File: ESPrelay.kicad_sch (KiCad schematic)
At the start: 26 parts, among them J1 Screw_Terminal, J3 USB_C_Receptacle_USB2.0_14P, K1 Relay_SPDT_Latching_1coil, K2 Relay_SPDT_Latching_1coil, K3 Relay_SPDT_Latching_1coil, K4 Relay_SPDT_Latching_1coil, K5 Relay_SPDT_Latching_1coil, K6 Relay_SPDT_Latching_1coil, K7 Relay_SPDT_Latching_1coil, K8 Relay_SPDT_Latching_1coil, U1 ESP32-S3-WROOM-1, U2 ULN2803A, U4 L7805, U5 LF33_TO252

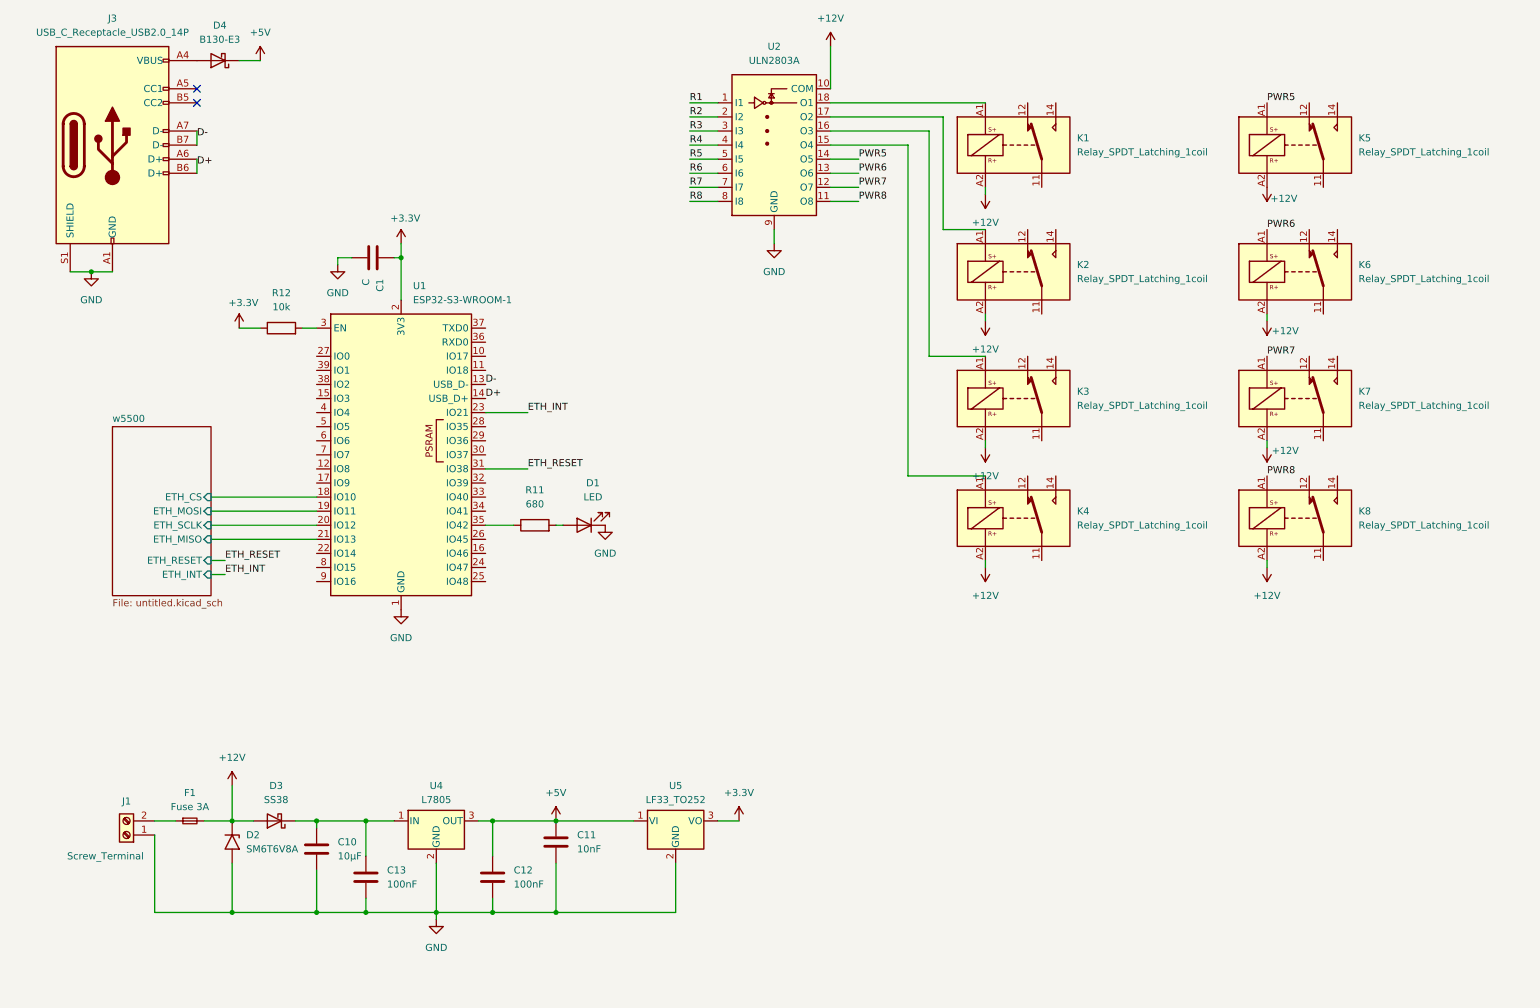
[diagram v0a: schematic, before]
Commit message: avancement carte 4 relays
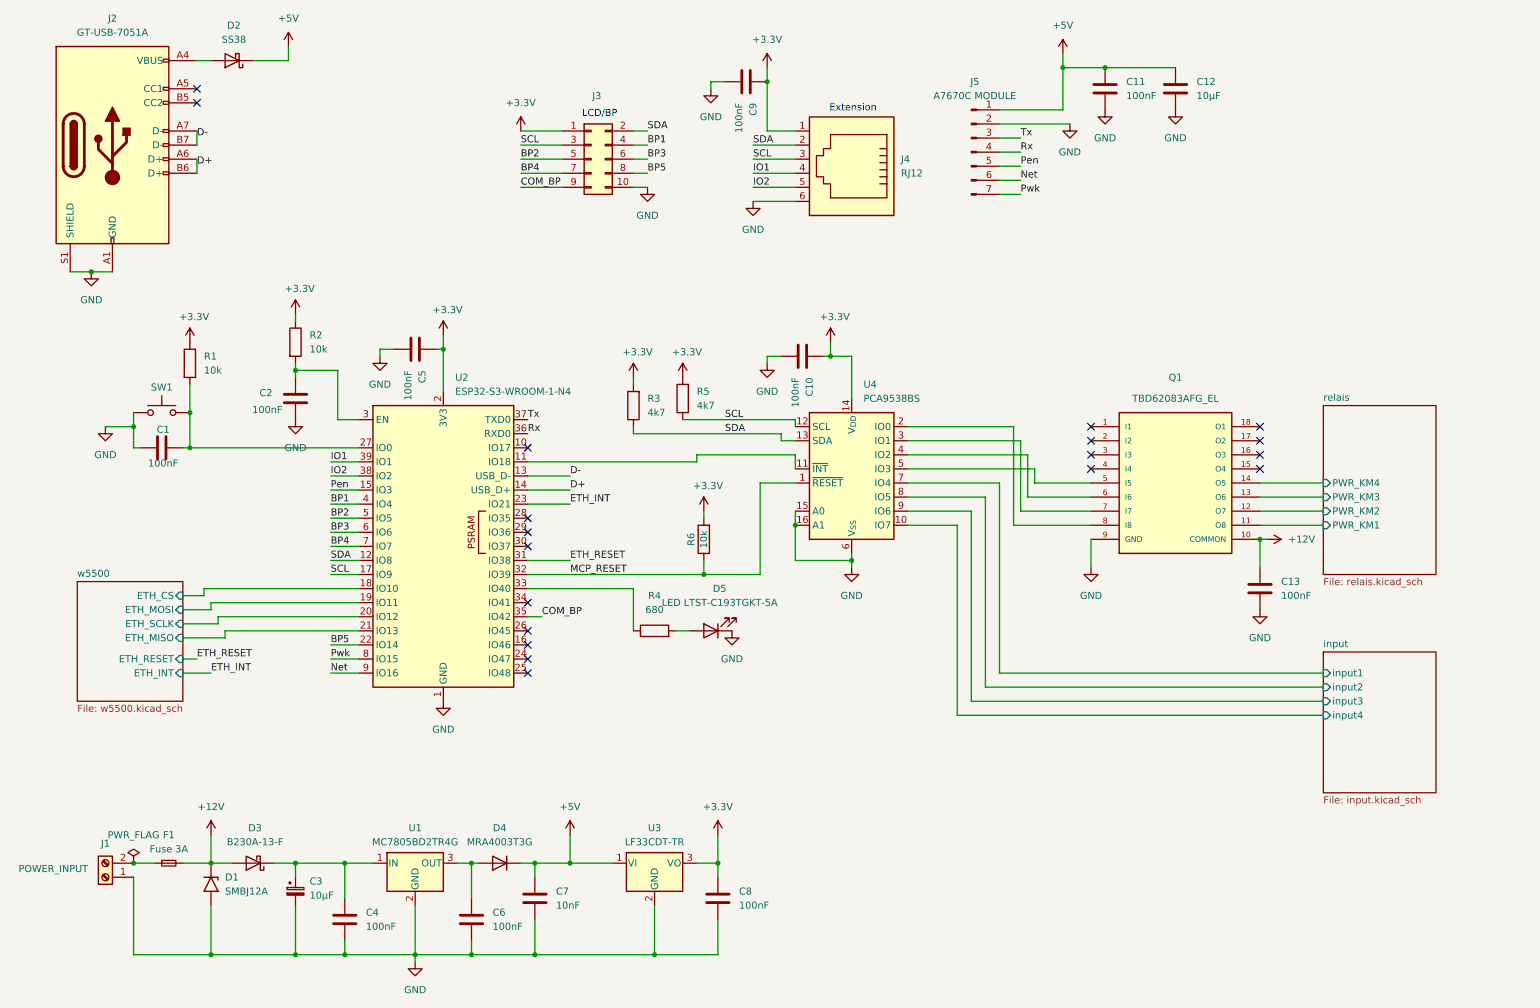
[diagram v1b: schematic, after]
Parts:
- removed D4: B130-E3, Diode_SMD:D_SMA, symbol Diode:B130-E3
- removed K1, K2, K3, K4, K5, K6, K7, K8: Relay_SPDT_Latching_1coil, Relay_THT:Relay_SPDT_Schrack-RP-II-1-FormC_RM3.5mm, symbol Relay:Relay_SPDT_Latching_1coil
- removed U2: ULN2803A, Package_SO:SOIC-18W_7.5x11.6mm_P1.27mm, symbol Transistor_Array:ULN2803A
- added C1, C11, C13, C2, C8, C9: 100nF, Capacitor_SMD:C_0402_1005Metric, symbol Device:C
- added C12: 10µF, Capacitor_SMD:C_0805_2012Metric, symbol Device:C
- added C3: 10µF, Capacitor_SMD:CP_Elec_4x5.4, symbol Device:C_Polarized_Small
- added D2: SS38, Diode_SMD:D_SMA, symbol Diode:SS38
- added D4: MRA4003T3G, Diode_SMD:D_SMA, symbol Diode:MRA4003T3G
- added J3: LCD/BP, Connector_FFC-FPC:Molex_54548-1071_1x10-1MP_P0.5mm_Horizontal, symbol Connector_Generic:Conn_02x05_Odd_Even
- added J4: RJ12, Connector_RJ:RJ12_Amphenol_54601-x06_Horizontal, symbol Connector:RJ12
- added J5: A7670C MODULE, labotronik:a7670c module, symbol Connector:Conn_01x07_Pin
- added Q1: TBD62083AFG_EL, TBD62083AFG_EL:SOIC127P1030X245-18N, symbol TBD62083AFG_EL:TBD62083AFG_EL
- added R1, R6: 10k, Resistor_SMD:R_0402_1005Metric, symbol Device:R
- added R3, R5: 4k7, Resistor_SMD:R_0402_1005Metric, symbol Device:R
- added SW1: SW_Push, Button_Switch_SMD:SW_Tactile_SPST_NO_Straight_CK_PTS636Sx25SMTRLFS, symbol Switch:SW_Push
- added U4: PCA9538BS, Package_DFN_QFN:NXP_VQFN-16-1EP_4x4mm_P0.65mm_EP2.1x2.1mm, symbol Interface_Expansion:PCA9538BS
- C10: value 10µF -> 100nF; footprint (none) -> Capacitor_SMD:C_0402_1005Metric
- C4: renamed from C13; footprint (none) -> Capacitor_SMD:C_0402_1005Metric
- C5: renamed from C1; value C -> 100nF; footprint Capacitor_SMD:C_0805_2012Metric -> Capacitor_SMD:C_0402_1005Metric
- C6: renamed from C12; footprint (none) -> Capacitor_SMD:C_0402_1005Metric
- C7: renamed from C11; footprint (none) -> Resistor_SMD:R_0402_1005Metric
- D1: renamed from D2; value SM6T6V8A -> SMBJ12A
- D3: value SS38 -> B230A-13-F
- D5: renamed from D1; value LED -> LED LTST-C193TGKT-5A; footprint (none) -> LED_SMD:LED_0603_1608Metric
- F1: footprint Fuse:Fuse_1210_3225Metric -> labotronik:0154250DR littelfuse 10.62 3.81
- J1: value Screw_Terminal -> POWER_INPUT; footprint TerminalBlock:TerminalBlock_MaiXu_MX126-5.0-02P_1x02_P5.00mm -> Connector_Phoenix_MC:PhoenixContact_MCV_1,5_2-G-3.5_1x02_P3.50mm_Vertical
- J2: renamed from J3; value USB_C_Receptacle_USB2.0_14P -> GT-USB-7051A; footprint Connector_USB:USB_C_Receptacle_G-Switch_GT-USB-7010ASV -> Connector_USB:USB_C_Receptacle_G-Switch_GT-USB-7051x
- R2: renamed from R12; footprint (none) -> Resistor_SMD:R_0402_1005Metric
- R4: renamed from R11; footprint (none) -> Resistor_SMD:R_0402_1005Metric
- U1: renamed from U4; value L7805 -> MC7805BD2TR4G
- U2: renamed from U1; value ESP32-S3-WROOM-1 -> ESP32-S3-WROOM-1-N4
- U3: renamed from U5; value LF33_TO252 -> LF33CDT-TR
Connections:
- net +12V: now also C13.1, Q1.10 (COMMON)
- net +3.3V: now also C10.1, C8.1, C9.1, J3.1 (Pin_1), J4.1, R1.1, R3.2, R5.2, R6.2, U4.14 (V_{DD})
- net +5V: now also C11.1, C12.1, D2.1 (K), D4.1 (K), J5.1 (Pin_1); no longer C6.1, U1.3 (OUT)
- net GND: now also C1.2, C11.2, C12.2, C13.2, C2.2, C3.2, C8.2, C9.2, J3.10 (Pin_10), J4.6, J5.2 (Pin_2), Q1.9 (GND), SW1.1, U4.15 (A0), U4.16 (A1), U4.17 (V_{SS}), U4.6 (V_{SS})
- net at U2.11 (IO18): now also U4.11 (~{INT})
- net SDA: now reaches U2.12 (IO8)
- net SDA: now also J3.2 (Pin_2), J4.2, R3.1, U4.13 (SDA)
- net Pen: now reaches U2.15 (IO3)
- net Pen: now also J5.5 (Pin_5)
- net SCL: now reaches U2.17 (IO9)
- net SCL: now also J3.3 (Pin_3), J4.3, R5.1, U4.12 (SCL)
- net BP5: now reaches U2.22 (IO14)
- net BP5: now also J3.8 (Pin_8)
- net at U2.27 (IO0): now also C1.1, R1.2, SW1.2
- net at R2.2, U2.3 (EN): now also C2.1
- net MCP_RESET: now reaches U2.32 (IO39)
- net MCP_RESET: now also R6.1, U4.1 (~{RESET})
- net at U2.33 (IO40): now also R4.1
- net COM_BP: now reaches U2.35 (IO42)
- net COM_BP: now also J3.9 (Pin_9); no longer R4.1
- net Rx: now reaches U2.36 (RXD0)
- net Rx: now also J5.4 (Pin_4)
- net Tx: now reaches U2.37 (TXD0)
- net Tx: now also J5.3 (Pin_3)
- net IO2: now reaches U2.38 (IO2)
- net IO2: now also J4.5
- net IO1: now reaches U2.39 (IO1)
- net IO1: now also J4.4
- net BP1: now reaches U2.4 (IO4)
- net BP1: now also J3.4 (Pin_4)
- net BP2: now reaches U2.5 (IO5)
- net BP2: now also J3.5 (Pin_5)
- net BP3: now reaches U2.6 (IO6)
- net BP3: now also J3.6 (Pin_6)
- net BP4: now reaches U2.7 (IO7)
- net BP4: now also J3.7 (Pin_7)
- net Pwk: now reaches U2.8 (IO15)
- net Pwk: now also J5.7 (Pin_7)
- net Net: now reaches U2.9 (IO16)
- net Net: now also J5.6 (Pin_6)
- net at J2.A4 (VBUS), J2.A9 (VBUS), J2.B4 (VBUS)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: now also D2.2 (A)
- net at C4.1, D3.1 (K), U1.1 (IN): now also C3.1; no longer C10.1
- new net: C6.1, D4.2 (A), U1.3 (OUT)
- new net: Q1.5 (I5), U4.5 (IO3)
- new net: Q1.6 (I6), U4.4 (IO2)
- new net: Q1.7 (I7), U4.3 (IO1)
- new net: Q1.8 (I8), U4.2 (IO0)
- new net input/input1: U4.7 (IO4)
- new net input/input2: U4.8 (IO5)
- new net input/input3: U4.9 (IO6)
- new net input/input4: U4.10 (IO7)
- new net relais/PWR_KM1: Q1.11 (O8)
- new net relais/PWR_KM2: Q1.12 (O7)
- new net relais/PWR_KM3: Q1.13 (O6)
- new net relais/PWR_KM4: Q1.14 (O5)
- no-connect marks 2 -> 19
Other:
- added sheet input (input.kicad_sch)
- added sheet relais (relais.kicad_sch)
- sheet w5500: file untitled.kicad_sch -> w5500.kicad_sch
- note added: "Extension"
- note added: "LCD/BP"
- moved on the sheet: C4, C5, C6, C7, D1, D3, D5, F1, J1, R2, R4, U1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

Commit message: update
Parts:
- removed D4: MRA4003T3G, Diode_SMD:D_SMA, symbol Diode:MRA4003T3G
- added D4: B230A-13-F, Diode_SMD:D_SMA, symbol Diode:SS38
- added JP2, JP3: SolderJumper_3_Bridged12, Jumper:SolderJumper-3_P1.3mm_Bridged12_RoundedPad1.0x1.5mm, symbol Jumper:SolderJumper_3_Bridged12
- D2: value SS38 -> B230A-13-F
- J3: value LCD/BP -> MOLEX 545480671
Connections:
- net +3.3V: now also JP2.3 (B), JP3.3 (B)
- net +5V: now also D4.1 (K)
- net GND: now also JP2.1 (A), JP3.1 (A); no longer U4.15 (A0), U4.16 (A1)
- net Rx: now also U2.37 (TXD0); no longer U2.36 (RXD0)
- net Tx: now also U2.36 (RXD0); no longer U2.37 (TXD0)
- net at C6.1, U1.3 (OUT): now also D2.2 (A)
- net at J2.A4 (VBUS), J2.A9 (VBUS), J2.B4 (VBUS)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: now also D4.2 (A); no longer D2.2 (A)
- new net: JP2.2 (C), U4.15 (A0)
- new net: JP3.2 (C), U4.16 (A1)
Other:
- moved on the sheet: D5, R4
